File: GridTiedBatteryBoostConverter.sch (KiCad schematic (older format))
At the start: 61 parts, among them J101 Battery Connection, J103 Solar Panels, Q101 IXFP36N20X3, Q102 BC847B-13-F, Q103 SSM3K329R, Q104 SSM3J334R, U101 OPA2837IDGKR, U102 UCC2800DTR

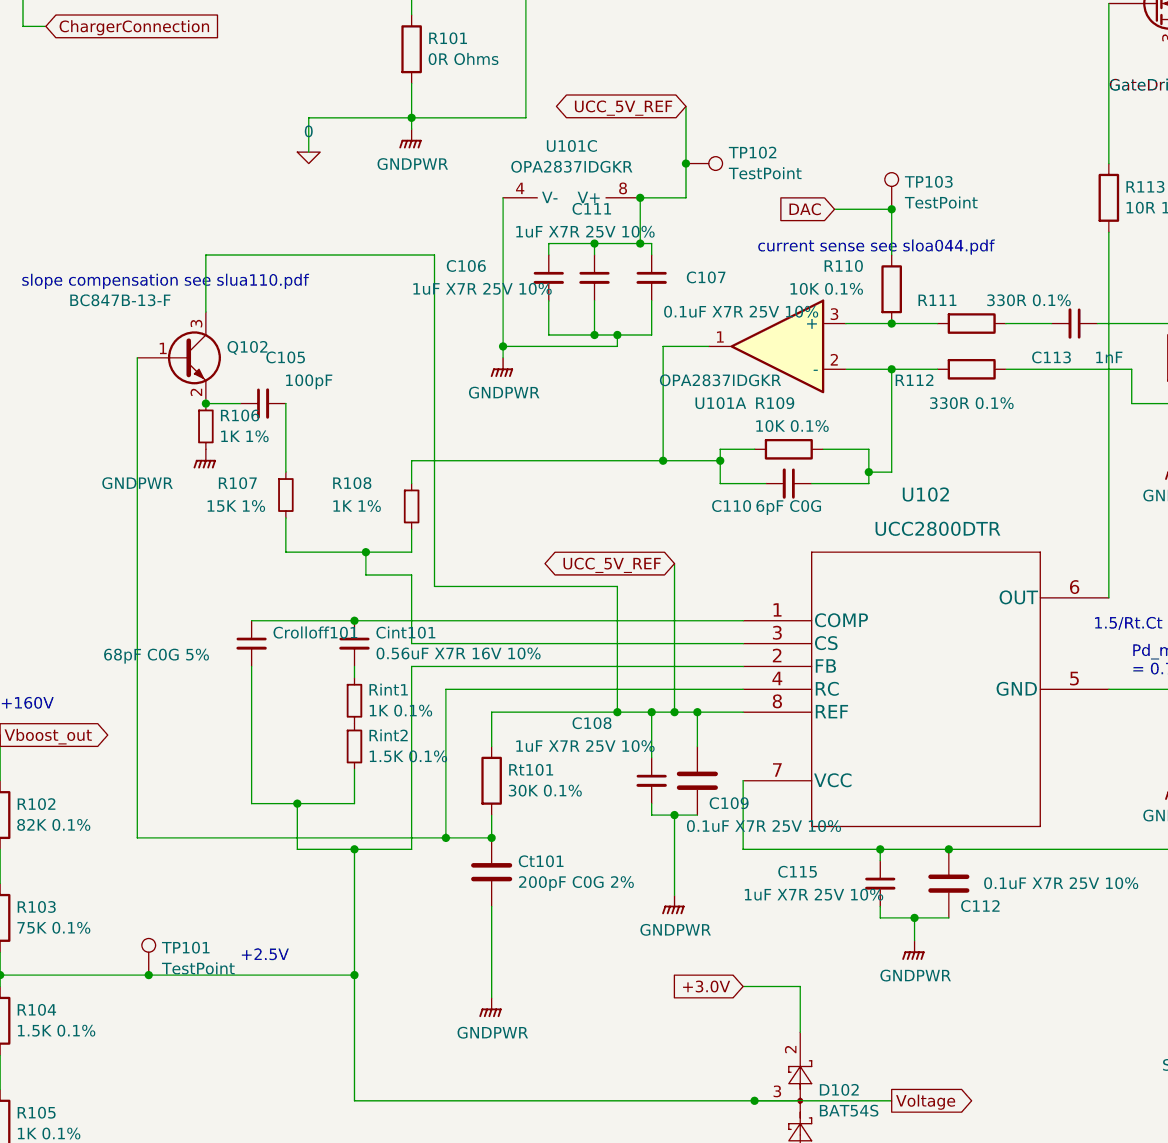
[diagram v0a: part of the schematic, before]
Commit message: Added extra FET in Current sense Auto Ranging circuit to stop the conduction of the body diode of the single FET on the negative half of the mains cycle.  Also change the Values of all the TestPoints from TestPoint to a useful name either the voltage they should read or what they measure, also chaged there layer to front Silks so they can be used.
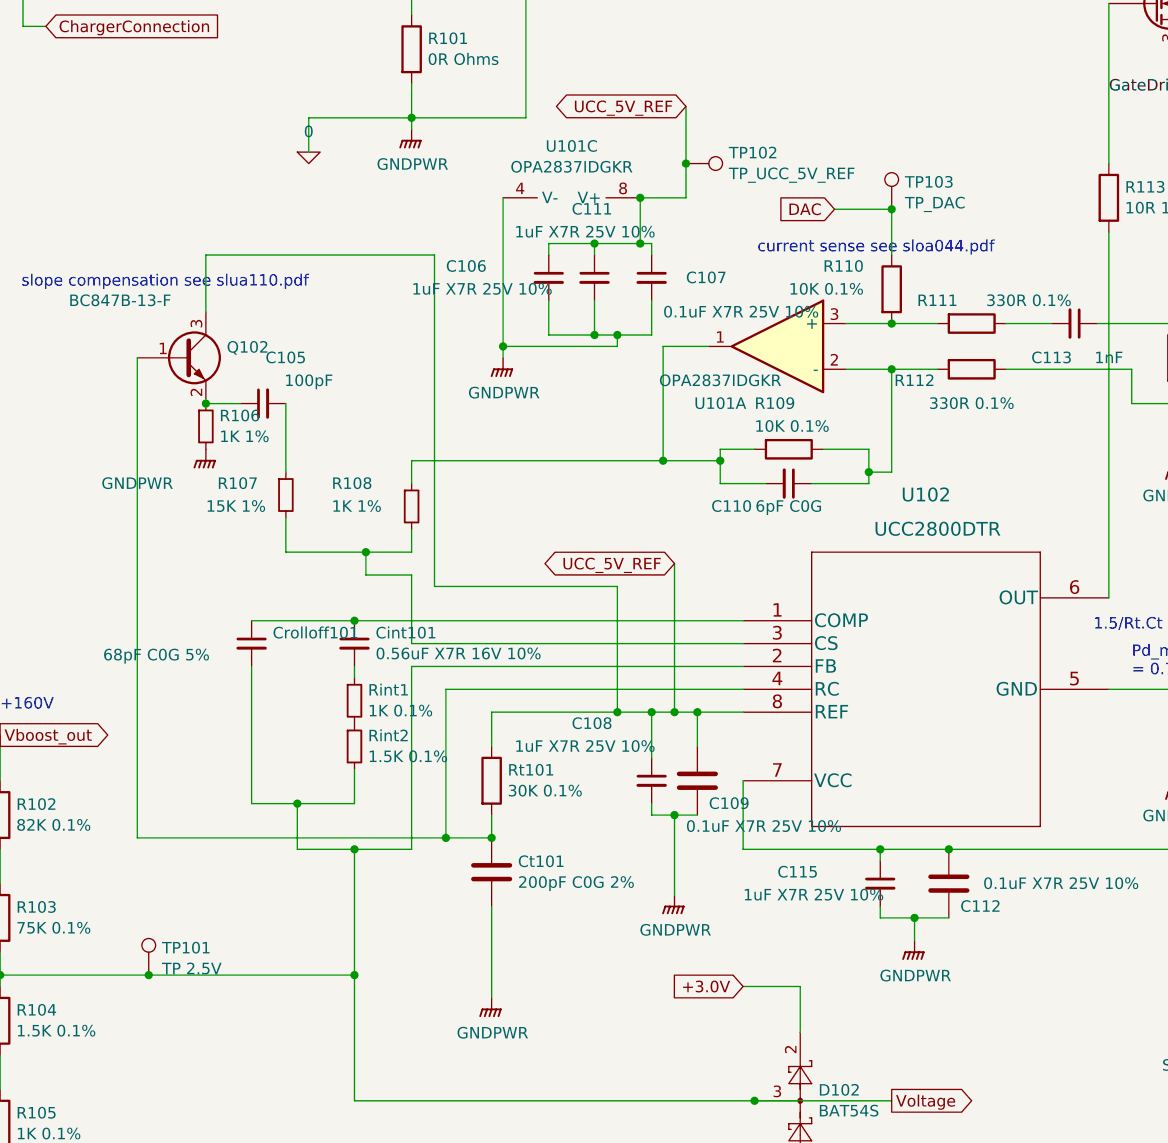
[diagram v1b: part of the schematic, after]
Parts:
- TP101: value TestPoint -> TP 2.5V
- TP102: value TestPoint -> TP_UCC_5V_REF
- TP103: value TestPoint -> TP_DAC
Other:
- note removed: "+2.5V"
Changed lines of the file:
@@
 AR Path="/6050D700" Ref="TP101"  Part="1"
 F 0 "TP101" H 1508 6418 50  0000 L CNN
-F 1 "TestPoint" H 1508 6327 50  0000 L CNN
+F 1 "TP 2.5V" H 1508 6327 50  0000 L CNN
 F 2 "TestPoint:TestPoint_Pad_3.0x3.0mm" H 1650 6300 50  0001 C CNN
 F 3 "~" H 1650 6300 50  0001 C CNN
@@
 AR Path="/60519D43" Ref="TP102"  Part="1"
 F 0 "TP102" V 3754 2938 50  0000 L CNN
-F 1 "TestPoint" V 3845 2938 50  0000 L CNN
+F 1 "TP_UCC_5V_REF" V 3845 2938 50  0000 L CNN
 F 2 "TestPoint:TestPoint_Pad_3.0x3.0mm" H 4000 2750 50  0001 C CNN
 F 3 "~" H 4000 2750 50  0001 C CNN
@@
 AR Path="/6051C0A5" Ref="TP103"  Part="1"
 F 0 "TP103" H 4758 3068 50  0000 L CNN
-F 1 "TestPoint" H 4758 2977 50  0000 L CNN
+F 1 "TP_DAC" H 4758 2977 50  0000 L CNN
 F 2 "TestPoint:TestPoint_Pad_3.0x3.0mm" H 4900 2950 50  0001 C CNN
 F 3 "~" H 4900 2950 50  0001 C CNN
@@
 Text Notes 5750 5000 0    50   ~ 0
 Pd_max=(125-40)/107.5 \n= 0.79W
-Text Notes 1850 6250 0    50   ~ 0
-+2.5V
 Text Notes 800  5150 0    50   ~ 0
 +160V
